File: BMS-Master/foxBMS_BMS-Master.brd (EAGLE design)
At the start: 160 x 120 mm, 314 parts, among them IC1001 AQV252G2S, IC1002 AQV252G2S, IC1003 AQV252G2S, IC1004 AQV252G2S, IC1005 AQV252G2S, IC1006 AQV252G2S, IC1101 UA78L05ACPK, IC1102 ADUM1300ARW, IC1103 ADUM1300ARW, IC1401 IP4220CZ6, IC1402 FT231XS-R, IC1403 ADUM1401ARW, IC1404 IP4220CZ6, IC1405 FT231XS-R, IC1406 ADUM1401ARW, IC1501 AT25128B-SSHL-T, IC1801 IS42S16400J-5TL, IC201 LM1085IS-5.0/NOPB, IC202 MURATA_NCS6S1205C, IC301 LM1085IS-5.0/NOPB, IC302 RS-2405D/H2, IC401 ADR3425ARJZ, IC402 STM32F429IIT6, IC501 STM32F429VIT6, IC601 ADUM1401ARW, IC701 UA78L05ACPK, IC702 ADUM1301ARW, IC801 KA7805ERTF, IC802 TJA1052IT/1Y, IC803 CPC1008N, IC901 LM317MBSTT3G, IC902 CPC1008N, IC903 CPC1008N, IC904 CPC1008N, IC905 CPC1008N, Q401 7B-8.000MAAJ-T, Q501 7B-8.000MAAJ-T, T1001 IRLML0100TRPBF, T1002 IRLML0100TRPBF, T1003 IRLML0100TRPBF, T1004 IRLML0100TRPBF, T1005 IRLML0100TRPBF, T1006 IRLML0100TRPBF, T401 BSS84P, T501 BSS84P, T701 IRLML0100TRPBF, T801 IRLML0100TRPBF, T901 BUK964R8-60E, T902 IRLML0100TRPBF, T903 IRLML0100TRPBF, X1201 43045-0400_MOLEX_4PIN, X1202 43045-0400_MOLEX_4PIN, X1203 43045-0400_MOLEX_4PIN, X1204 43045-0400_MOLEX_4PIN, X1205 43045-0400_MOLEX_4PIN, X1206 43045-0400_MOLEX_4PIN, X1401 MINI-USB-2.0, X1402 MINI-USB-2.0, X1601 43045-1600_MOLEX_16PIN, X201 43045-0600_MOLEX_6PIN, X402 MA02-1, X403 SAMTEC_FTS_20POL_HEADER_VERTI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, X501 MA02-1, X502 SAMTEC_FTS_20POL_HEADER_VERTI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, X701 43045-0400_MOLEX_4PIN, X801 43045-0400_MOLEX_4PIN, X901 43045-0200_MOLEX_2PIN, X902 MA02-1SMALL_PINS_OUTLINE

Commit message: Minor updates and corrections of notations, wording and bill of materials (V1.0.1). No changes in schematic and layout.
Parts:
- removed D301: VS-10BQ040-M3, 0_LES_DIODE.SMD.SCHOTTKY:D_SMD_SMB_(DO-214AA)_R_VISHAY_REV01
- added F201: 0,500A_LITTELFUSE_4482A, foxBMS_BMS-Master:448_SERIES_LITTELFUSE
- added T201: TISP40XXH1BJ, foxBMS_BMS-Master:TVS_THYRISTOR
- added U$1, U$3, U$4: (no value), foxBMS_BMS-Slave_12cell:FIDUCIAL_1MM
- BATT: device 0_LES_MECHANIK.SMD:X_SMD_(23,70MM_X_12,70MM_X_5,00MM)_R_RENATA_REV01 -> foxBMS_BMS-Master:X_SMD_(23,70MM_X_12,70MM_X_5,00MM)_R_RENATA_REV01
- C1101, C1102, C1103, C1104, C1105, C1106, C1107, C1401, C1402, C1403, C1404, C1405, C1406, C1407, C1408, C1409, C1410, C1601, C1602, C1603, C1604, C1801, C1802, C1803, C1804, C1805, C1806, C1807, C202, C205, C206, C207, C208, C2101, C2102, C301, C305, C306, C307, C308, C401, C402, C403, C404, C405, C406, C407, C408, C409, C410, C411, C412, C413, C414, C415, C416, C417, C418, C419, C420, C421, C422, C423, C424, C425, C426, C427, C428, C429, C430, C501, C502, C503, C504, C505, C506, C507, C508, C509, C510, C511, C512, C513, C601, C602, C701, C702, C703, C704, C705, C706, C707, C902: device rcl:C0603 -> foxBMS_BMS-Master:C0603
- C1501, C801, C802, C803, C804, C805, C806, C807, R1401, R1402, R1403, R1404, R1405, R1406, R1407, R1408, R1501, R1502, R803, R804, R805, R806: device custom_passiv:0603 -> foxBMS_BMS-Master:0603
- C201, C203, C204, C302, C303, C304, C901: device rcl:C0805 -> foxBMS_BMS-Master:C0805
- D1001, D1002, D1003, D1004, D1005, D1006: device diode:SMA-DO214AC -> foxBMS_BMS-Master:SMA-DO214AC
- D1101, D1102, D1103, D1104, D1105, D1106: device 0_LES_TVS.SMD.ARRAY:D_SMD_SOD323_(SC-76)_R_BOURNS_REV01 -> foxBMS_BMS-Master:D_SMD_SOD323_(SC-76)_R_BOURNS_REV01
- D201: device 0_LES_DIODE.SMD.SCHOTTKY:D_SMD_SMB_(DO-214AA)_R_VISHAY_REV01 -> foxBMS_BMS-Master:D_SMD_SMB_(DO-214AA)_R_VISHAY_REV01
- D701, D702: device custom_diode:SOD323 -> foxBMS_BMS-Master:SOD323
- D801: device 0_LES_TVS.SMD.ARRAY:D_SMD_SOT23_(TO-236AB)_R_NXP_REV01 -> foxBMS_BMS-Master:D_SMD_SOT23_(TO-236AB)_R_NXP_REV01
- D901, D902: device foxBMS_BMS-Master_V1.00_A:SOD323 -> foxBMS_BMS-Master:SOD323
- F1001, F1002, F1003, F1004, F1005, F1006: device 0_LES_SICHERUNG.SMD:F_SMD_11,00MMX3,00MMX3,00MM_(UMT)_R_SCHURTER_REV01 -> foxBMS_BMS-Master:F_SMD_11,00MMX3,00MMX3,00MM_(UMT)_R_SCHURTER_REV01
- IC1001, IC1002, IC1003, IC1004, IC1005, IC1006: device 0_LES_RELAIS.SMD:K_SMD_SOP-6_R_PANASONIC_REV01 -> foxBMS_BMS-Master:K_SMD_SOP-6_R_PANASONIC_REV01
- IC1101, IC701: device 0_LES_SPANNUNGSREGLER.SMD.LINEAR.EINZEL:IC_SMD_SOT-89_(SC-62/TO-243)_(R-PSSO-F3)_R_TI_REV01 -> foxBMS_BMS-Master:IC_SMD_SOT-89_(SC-62/TO-243)_(R-PSSO-F3)_R_TI_REV01
- IC1401, IC1404: device 0_LES_TVS.SMD.ARRAY:D_SMD_TSOP6_(SOT457/SC-74)_R_NXP_REV01 -> foxBMS_BMS-Master:D_SMD_TSOP6_(SOT457/SC-74)_R_NXP_REV01
- IC1402, IC1405: device 0_LES_SCHNITTSTELLEN-IC.SMD.USB-TRANSCEIVER:IC_SMD_SSOP-20_R_FTDI_REV01 -> foxBMS_BMS-Master:IC_SMD_SSOP-20_R_FTDI_REV01
- IC1403, IC1406, IC601: device 0_LES_SCHNITTSTELLEN-IC.SMD.ISOLATOR:IC_SMD_SOIC-16_(JEDEC_MS-013-AA)_R_ANALOG_REV01 -> foxBMS_BMS-Master:IC_SMD_SOIC-16_(JEDEC_MS-013-AA)_R_ANALOG_REV01
- IC1501: device 0_LES_SPEICHER.SMD.EEPROM:IC_SMD_SOIC-8_R_ATMEL_REV01 -> foxBMS_BMS-Master:IC_SMD_SOIC-8_R_ATMEL_REV01
- IC1801: device 0_LES_SPEICHER.SMD.SDRAM:IC_SMD_TSOP-II_(54-PIN)_R_ISSI_REV01 -> foxBMS_BMS-Master:IC_SMD_TSOP-II_(54-PIN)_R_ISSI_REV01
- IC201, IC301: device 0_LES_SPANNUNGSREGLER.SMD.LINEAR.EINZEL:IC_SMD_TO-263-3_(KTT0003B)_R_TI_REV01 -> foxBMS_BMS-Master:IC_SMD_TO-263-3_(KTT0003B)_R_TI_REV01
- IC202: device 0_LES_SPANNUNGSWANDLER.TH.DC-DC.EINZEL.ISOLIERT:IC_TH_32,00MMX20,00MMX10,00MM_(7-PIN)_R_MURATA_REV01 -> foxBMS_BMS-Master:IC_TH_32,00MMX20,00MMX10,00MM_(7-PIN)_R_MURATA_REV01
- IC302: device 0_LES_SPANNUNGSWANDLER.TH.DC-DC.MULTI.ISOLIERT:IC_TH_SIP8_R_RECOM_REV01 -> foxBMS_BMS-Master:IC_TH_SIP8_R_RECOM_REV01
- IC401: device 0_LES_VREF.SMD.SERIELL:IC_SMD_SOT23-6_(MO-178-AB)_R_AD_REV01 -> foxBMS_BMS-Master:IC_SMD_SOT23-6_(MO-178-AB)_R_AD_REV01
- IC402: device 0_LES_MCU.SMD.32BIT:IC_SMD_LQFP176_R_ST_REV01 -> foxBMS_BMS-Master:IC_SMD_LQFP176_R_ST_REV01
- IC501: device 0_LES_MCU.SMD.32BIT:IC_SMD_LQFP100_R_ST_REV01 -> foxBMS_BMS-Master:IC_SMD_LQFP100_R_ST_REV01
- IC801: device 0_LES_SPANNUNGSREGLER.SMD.LINEAR.EINZEL:IC_SMD_TO-252_(D-PAK)_R_FAIRCHILD_REV01 -> foxBMS_BMS-Master:IC_SMD_TO-252_(D-PAK)_R_FAIRCHILD_REV01
- IC802: device 0_LES_SCHNITTSTELLEN-IC.SMD.CAN-TRANSCEIVER:IC_SMD_SO16_(SOT162-1)_R_NXP_REV01 -> foxBMS_BMS-Master:IC_SMD_SO16_(SOT162-1)_R_NXP_REV01
- IC803, IC902, IC903, IC904, IC905: device 0_LES_RELAIS.SMD:K_SMD_SOP-4_R_IXYS_REV01 -> foxBMS_BMS-Master:K_SMD_SOP-4_R_IXYS_REV01
- IC901: device 0_LES_SPANNUNGSREGLER.SMD.LINEAR.EINZEL:IC_SMD_SOT-223_(TO-261)_(CASE318E-04)_R_REV01 -> foxBMS_BMS-Master:IC_SMD_SOT-223_(TO-261)_(CASE318E-04)_R_REV01
- JP2201, JP2202: device foxBMS_BMS-Master_BasicBoard_V1.02_A:2X12 -> foxBMS_BMS-Master:2X12
- L401: device foxBMS_BMS-Master_V1.00_A:0805 -> foxBMS_BMS-Master:0805
- L801: device 0_LES_INDUKTIVITAET.SMD.FILTER.HF:L_SMD_FILTER_HF_R_EPCOS_SIMDAD_1812_REV01 -> foxBMS_BMS-Master:L_SMD_FILTER_HF_R_EPCOS_SIMDAD_1812_REV01
- LED201, LED301, LED401, LED402, LED501, LED502: device led:CHIP-LED0603 -> foxBMS_BMS-Master:CHIP-LED0603
- Q401, Q501: device 0_LES_CRYSTAL.SMD.XO:G_SMD_5,00MM_X_3,20MM_0,90MM_(7B)_TXC_REV01 -> foxBMS_BMS-Master:G_SMD_5,00MM_X_3,20MM_0,90MM_(7B)_TXC_REV01
- Q402: device foxBMS_BMS-Master_V1.00_A:MS3V-T1R -> foxBMS_BMS-Master:MS3V-T1R
- R1001, R1002, R1003, R1004, R1005, R1006, R1007, R1008, R1009, R1010, R1011, R1012, R1013, R1014, R1015, R1016, R1017, R1018, R1101, R1102, R1103, R1104, R1105, R1106, R1107, R1108, R1109, R1110, R1111, R1112, R201, R301, R401, R402, R403, R404, R405, R406, R407, R408, R409, R501, R502, R503, R504, R505, R506, R507, R508, R509, R701, R702, R703, R704, R705, R706, R707, R708, R709, R710, R901, R902, R903, R904, R905, R906, R907, R908, R909, R910, R911, R912: device rcl:R0603 -> foxBMS_BMS-Master:R0603
- R801, R802: device custom_passiv:0603 -> rcl:R0603
- S401, S501: device 0_LES_SCHALTER-TASTER.SMD:S_SMD_4,60MMX2,80MMX1,90MM_R_CK-COMPONENTS_REV01 -> foxBMS_BMS-Master:S_SMD_4,60MMX2,80MMX1,90MM_R_CK-COMPONENTS_REV01
- SV1601, SV1603, SV2101, SV901: device foxBMS_BMS-Master_BasicBoard_V1.02_A:MA04-2 -> foxBMS_BMS-Master:MA04-2
- SV1602, SV1604: device foxBMS_BMS-Master_BasicBoard_V1.02_A:MA08-2 -> foxBMS_BMS-Master:MA08-2
- SV501: device foxBMS_BMS-Master_BasicBoard_V1.02_A:MA06-2 -> foxBMS_BMS-Master:MA06-2
- T1001, T1002, T1003, T1004, T1005, T1006, T701, T801, T902, T903: device 0_LES_TRANSISTOR.SMD.MOS.N-KANAL.NO:V_SMD_SOT-23_(TO-236AB)_R_IR_REV01 -> foxBMS_BMS-Master:V_SMD_SOT-23_(TO-236AB)_R_IR_REV01
- T401, T501: device 0_LES_TRANSISTOR.SMD.MOS.P-KANAL.NO:V_SMD_SOT23_(TO-236AB)_R_INFINEON_REV01 -> foxBMS_BMS-Master:V_SMD_SOT23_(TO-236AB)_R_INFINEON_REV01
- T901: device 0_LES_TRANSISTOR.SMD.MOS.N-KANAL.NO:V_SMD_TO-263_(D²PAK)_R_NXP_REV01 -> foxBMS_BMS-Master:V_SMD_TO-263_(D²PAK)_R_NXP_REV01
- TP_GND_201, TP_GND_301: device wirepad:1,6/0,8 -> foxBMS_BMS-Master:1,6/0,8
- X1201, X1202, X1203, X1204, X1205, X1206, X701, X801: device 0_LES_STECKVERBINDUNG.TH.RASTER_3,00MM.BUCHSE:X_TH_MOLEX_43045-0400_R_REV01 -> foxBMS_BMS-Master:X_TH_MOLEX_43045-0400_R_REV01
- X1601: device 0_LES_STECKVERBINDUNG.TH.RASTER_3,00MM.BUCHSE:X_TH_MOLEX_43045-1600_R_REV01 -> foxBMS_BMS-Master:X_TH_MOLEX_43045-1600_R_REV01
- X201: device 0_LES_STECKVERBINDUNG.TH.RASTER_3,00MM.BUCHSE:X_TH_MOLEX_43045-0600_R_REV01 -> foxBMS_BMS-Master:X_TH_MOLEX_43045-0600_R_REV01
- X401: device foxBMS_BMS-Master_BasicBoard_V1.02_A:MA03-1 -> foxBMS_BMS-Master:MA03-1
- X402, X501: device foxBMS_BMS-Master_BasicBoard_V1.02_A:MA02-1 -> foxBMS_BMS-Master:MA02-1
- X403, X502: device 0_LES_STECKVERBINDUNG.SMD.RASTER_1,27MM.STECKER:X_SMD_FTS_110-03_(20POL)_R_SAMTEC_REV01 -> foxBMS_BMS-Master:X_SMD_FTS_110-03_(20POL)_R_SAMTEC_REV01
- X901: device 0_LES_STECKVERBINDUNG.TH.RASTER_3,00MM.BUCHSE:X_TH_MOLEX_43045-0200_R_REV01 -> foxBMS_BMS-Master:X_TH_MOLEX_43045-0200_R_REV01
- X902: device foxBMS_BMS-Master_BasicBoard_V1.02_A:MA02-1A -> foxBMS_BMS-Master:MA02-1A
- moved D201 0.71 mm to (155.3, -29.5)
- moved X401 0.16 mm to (57.9, -68.7)
- moved X402 0.16 mm to (67.5, -68.7)
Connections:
- removed net N$270: C201.1, C203.1, C204.1, D201.C, IC202.22, IC202.23
- removed net N$34: C302.1, C303.1, C304.1, D301.C, IC302.2
- new net N$16: D201.A, F201.P$2, T201.A
- new net N$17: F201.P$1, X201.4
- net GND_EXT_0: now also T201.C
- net SUPPLY_EXT_0: now also C201.1, C203.1, C204.1, C302.1, C303.1, C304.1, D201.C, IC202.22, IC202.23, IC302.2; no longer D201.A, D301.A, X201.4
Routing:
- net SUPPLY_EXT_0: track 31.6 -> 85.0 mm, vias 15 -> 9
- net N$270: track 28.3 -> 0.00 mm
- net N$16: track 0.00 -> 27.8 mm, vias 0 -> 13
- net N$34: track 24.3 -> 0.00 mm
- net GND_EXT_0: track 128.5 -> 119.2 mm, vias 48 -> 53
- net N$17: track 0.00 -> 5.03 mm
- added copper zone on layer 1, net N$16
- added copper zone on layer 16, net N$16
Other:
- board text added: "Fuse: 2A"
- board text added: "foxBMS BMS-Master V1.0.1"
- board text removed: "Fraunhofer IISB L21584"
- board text removed: "foxBMS BMS-Master Basic V1.00"

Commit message: Changed ADUM1xxx to ADUM3xxx in schematic of BMS-Master and BMS-Extension
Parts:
- IC1102, IC1103: value ADUM1300ARW -> ADUM3300ARW; device 0_LES_SCHNITTSTELLEN-IC.SMD.ISOLATOR:IC_SMD_SOIC-16_(JEDEC_MS-013-AA)_R_ANALOG_REV01 -> foxBMS_BMS-Master:IC_SMD_SOIC-16_(JEDEC_MS-013-AA)_R_ANALOG_REV01
- IC1403, IC1406, IC601: value ADUM1401ARW -> ADUM3401ARW
- IC702: value ADUM1301ARW -> ADUM3301ARW; device 0_LES_SCHNITTSTELLEN-IC.SMD.ISOLATOR:IC_SMD_SOIC-16_(JEDEC_MS-013-AA)_R_ANALOG_REV01 -> foxBMS_BMS-Master:IC_SMD_SOIC-16_(JEDEC_MS-013-AA)_R_ANALOG_REV01
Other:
- board text added: "foxBMS BMS-Master V1.0.2"
- board text removed: "foxBMS BMS-Master V1.0.1"

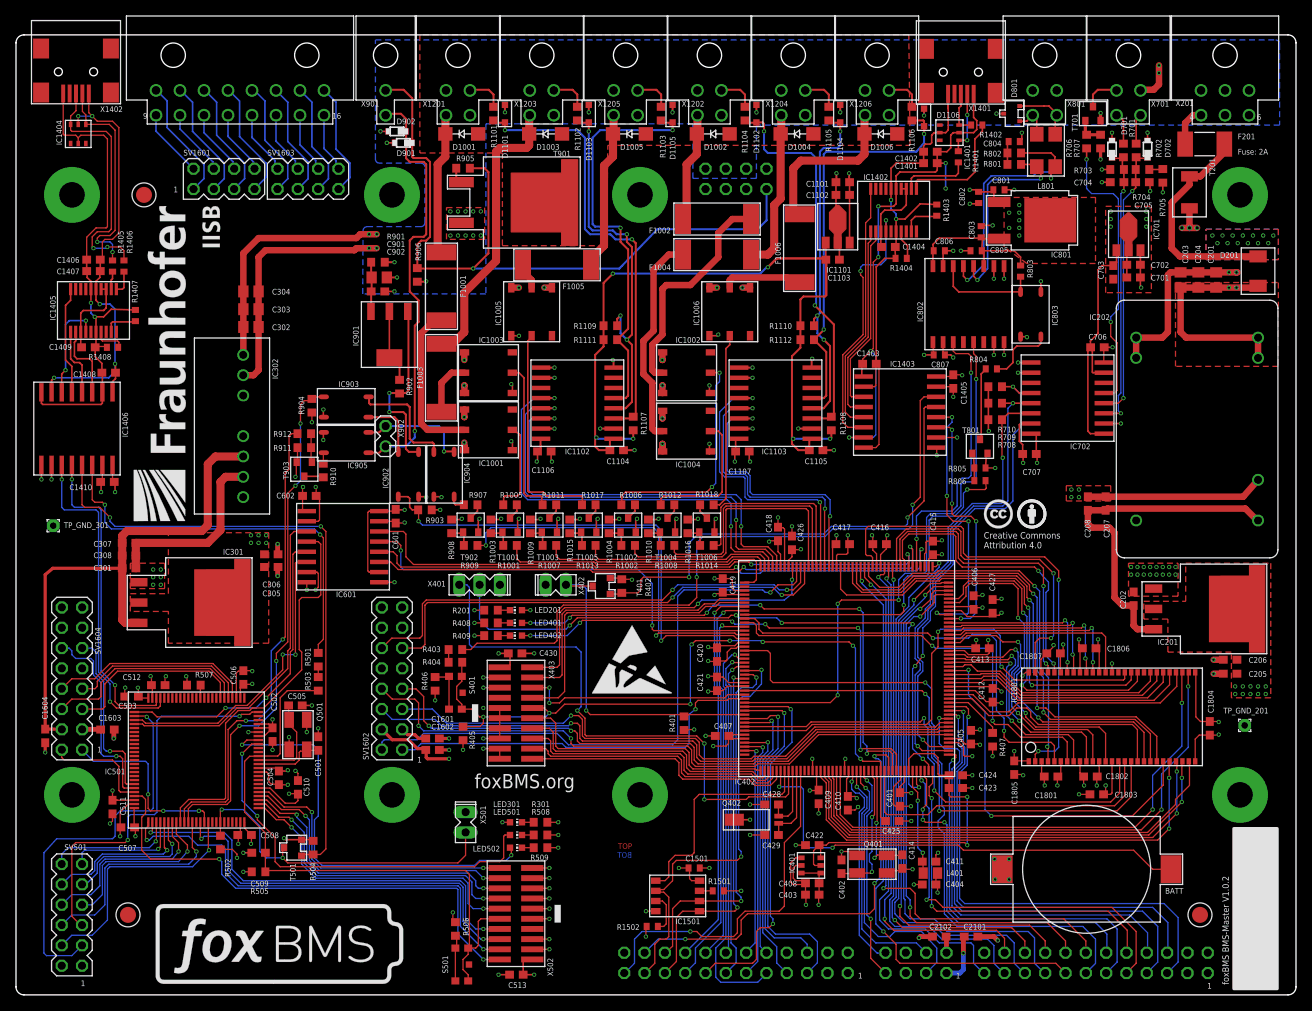
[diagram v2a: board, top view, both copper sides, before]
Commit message: updated foxBMS-slave to version 2.02
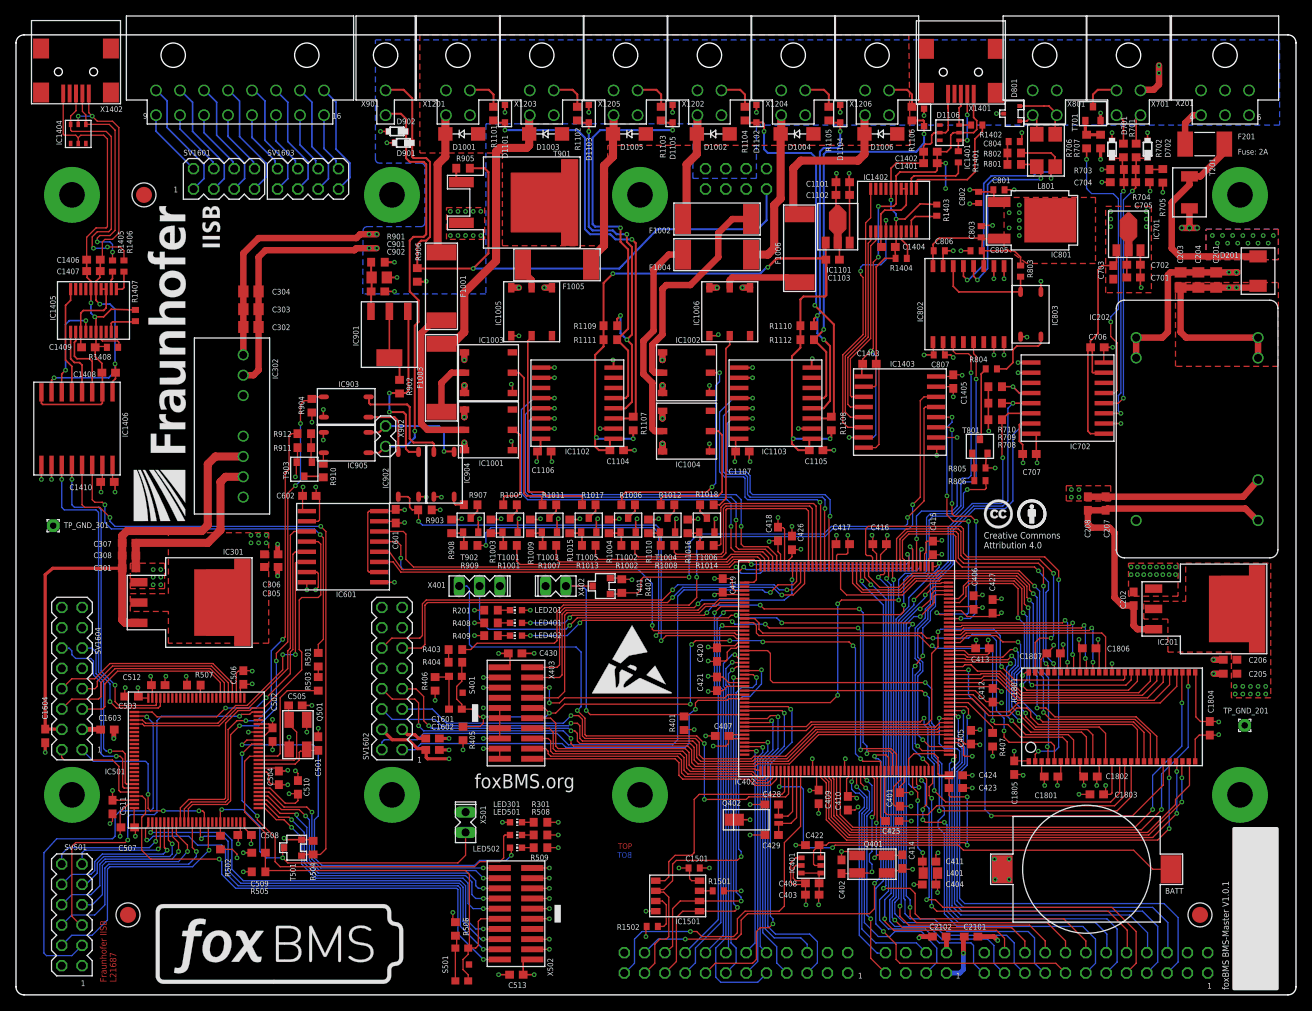
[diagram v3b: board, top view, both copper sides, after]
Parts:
- IC1102, IC1103: value ADUM3300ARW -> ADUM1300ARW; device foxBMS_BMS-Master:IC_SMD_SOIC-16_(JEDEC_MS-013-AA)_R_ANALOG_REV01 -> 0_LES_SCHNITTSTELLEN-IC.SMD.ISOLATOR:IC_SMD_SOIC-16_(JEDEC_MS-013-AA)_R_ANALOG_REV01
- IC1403, IC1406, IC601: value ADUM3401ARW -> ADUM1401ARW
- IC702: value ADUM3301ARW -> ADUM1301ARW; device foxBMS_BMS-Master:IC_SMD_SOIC-16_(JEDEC_MS-013-AA)_R_ANALOG_REV01 -> 0_LES_SCHNITTSTELLEN-IC.SMD.ISOLATOR:IC_SMD_SOIC-16_(JEDEC_MS-013-AA)_R_ANALOG_REV01
- moved X401 0.16 mm to (57.9, -68.9)
- moved X402 0.16 mm to (67.5, -68.9)
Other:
- board text added: "Fraunhofer IISB L21584"
- board text added: "Fraunhofer IISB L21687"
- board text added: "foxBMS BMS-Master V1.0.1"
- board text removed: "foxBMS BMS-Master V1.0.2"
